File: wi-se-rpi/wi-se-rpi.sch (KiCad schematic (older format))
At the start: 43 parts, among them J1 RASPI, SW1 RESET, SW2 BOOT0, SW3 FLASH_EN_SW, U1 AMS1117-3.3, U2 ESP-WROOM-02, U3 MC74VHC1G, U4 NL27WZ00, U5 NL27WZ32

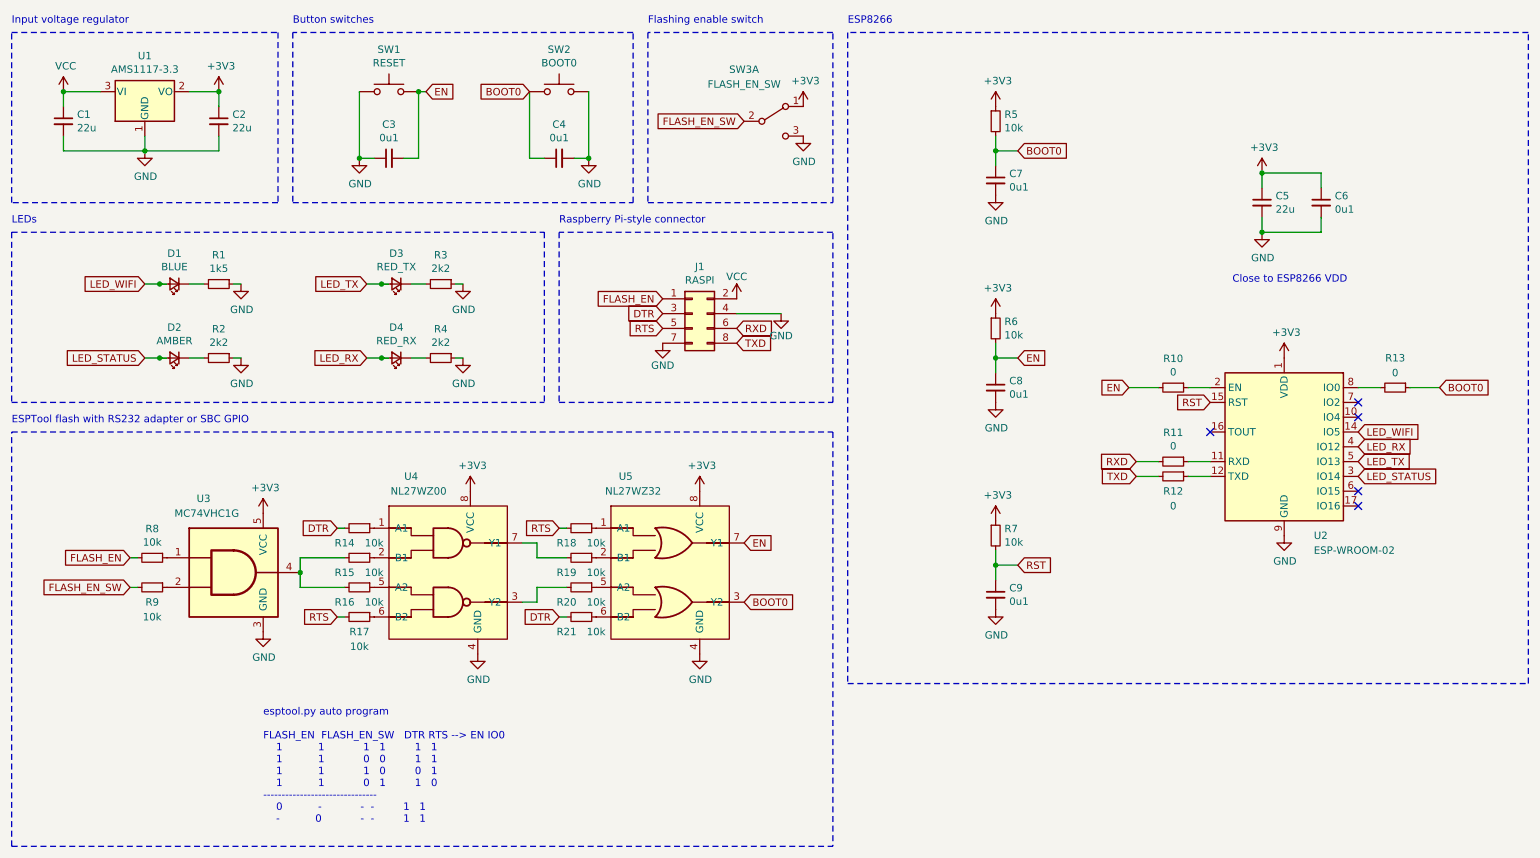
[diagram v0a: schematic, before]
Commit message: Make RPI version as small as it can be
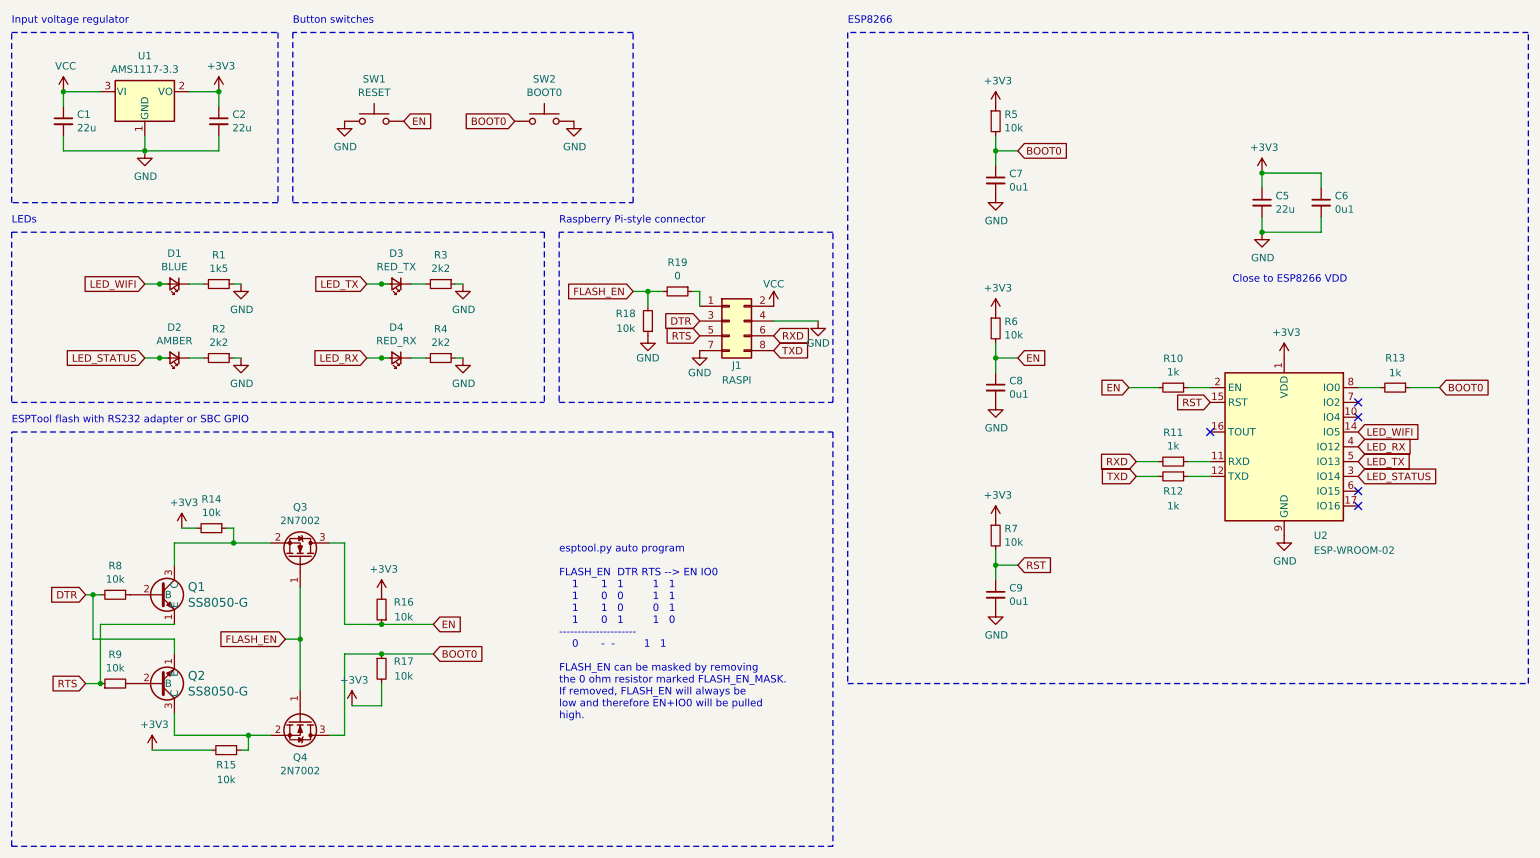
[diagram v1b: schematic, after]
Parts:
- removed C3, C4: 0u1, Capacitor_SMD:C_0603_1608Metric_Pad1.08x0.95mm_HandSolder, symbol Device:C_Small
- removed R20, R21: 10k, Resistor_SMD:R_0603_1608Metric_Pad0.98x0.95mm_HandSolder, symbol Device:R_Small
- removed SW3: FLASH_EN_SW, JS102011SCQN:CK-JS102011SCQN-0-0-0, symbol Switch:SW_DPDT_x2
- removed U3: MC74VHC1G, ON-gates:SOT95P280X145-5N, symbol Logic_Gates:MC74VHC1G
- removed U4: NL27WZ00, ON-gates:SOP50P310X90-8N, symbol Logic_Gates:NL27WZ00
- removed U5: NL27WZ32, ON-gates:SOP50P310X90-8N, symbol Logic_Gates:NL27WZ32
- added Q1, Q2: SS8050-G, SS8050-G:SS8050-G, symbol SS8050-G:SS8050-G
- added Q3, Q4: 2N7002, Package_TO_SOT_SMD:SOT-23, symbol Transistor_FET:2N7002
- C1, C2, C5: footprint Capacitor_SMD:C_1206_3216Metric_Pad1.33x1.80mm_HandSolder -> Capacitor_SMD:C_1206_3216Metric
- C6: footprint Capacitor_SMD:C_0603_1608Metric_Pad1.08x0.95mm_HandSolder -> Capacitor_SMD:C_0603_1608Metric
- C7, C8, C9: footprint Capacitor_SMD:C_0603_1608Metric_Pad1.08x0.95mm_HandSolder -> Capacitor_SMD:C_0402_1005Metric
- R1, R14, R15, R16, R17, R18, R2, R3, R4, R5, R6, R7, R8, R9: footprint Resistor_SMD:R_0603_1608Metric_Pad0.98x0.95mm_HandSolder -> Resistor_SMD:R_0402_1005Metric
- R10, R11, R12, R13: value 0 -> 1k; footprint Resistor_SMD:R_0603_1608Metric_Pad0.98x0.95mm_HandSolder -> Resistor_SMD:R_0402_1005Metric
- R19: value 10k -> 0
- SW1, SW2: footprint Button_Switch_SMD:SW_SPST_B3U-3100P -> wi-se:SW_SPST_B3U-3100P_silk_change
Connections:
- net labels removed: FLASH_EN_SW
- wire segments 74 -> 87
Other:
- note added: "esptool.py auto program\n\nFLASH_EN DTR RTS --> EN IO0\n 1 1 1 1 1\n 1 0 0 1 1\n 1 1 0 0 1\n 1 0 1 1 0\n---------------------\n 0 - - 1 1 \n\nFLASH_EN can be masked by removing\nthe 0 ohm resistor marked FLASH_EN_MASK.\nIf removed, FLASH_EN will always be\nlow and therefore EN+IO0 will be pulled\nhigh."
- note removed: "Flashing enable switch"
- note removed: "esptool.py auto program\n\nFLASH_EN FLASH_EN_SW DTR RTS --> EN IO0\n 1 1 1 1 1 1\n 1 1 0 0 1 1\n 1 1 1 0 0 1\n 1 1 0 1 1 0\n-------------------------------\n 0 - - - 1 1\n - 0 - - 1 1\n"
- moved on the sheet: J1, SW1, SW2

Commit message: Final version of rpi variant (last famous words)
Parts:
- C1, C2, C5: value 22u -> 10u; LCSC Part (none) -> C13585
- C6: LCSC Part (none) -> C14663
- C7, C8, C9: LCSC Part (none) -> C1546
- Q1, Q2: LCSC Part (none) -> C2150
- Q3, Q4: LCSC Part (none) -> C8545
- R1: LCSC Part (none) -> C25867
- R10, R11, R12, R13: LCSC Part (none) -> C11702
- R14, R15, R16, R17, R18, R5, R6, R7, R8, R9: LCSC Part (none) -> C25744
- R19: LCSC Part (none) -> C17168
- R2, R3, R4: LCSC Part (none) -> C25879
- U1: LCSC Part (none) -> C6186
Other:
- note added: "esptool.py auto program\n\nFLASH_EN DTR RTS --> EN IO0\n 1 1 1 1 1\n 1 0 0 1 1\n 1 1 0 0 1\n 1 0 1 1 0\n---------------------\n 0 - - 1 1 \n\nFLASH_EN can be masked by removing\nthe 0 ohm resistor marked "FLEN disable".\nIf removed, FLASH_EN will always be\nlow and therefore EN+IO0 will be pulled\nhigh."
- note removed: "esptool.py auto program\n\nFLASH_EN DTR RTS --> EN IO0\n 1 1 1 1 1\n 1 0 0 1 1\n 1 1 0 0 1\n 1 0 1 1 0\n---------------------\n 0 - - 1 1 \n\nFLASH_EN can be masked by removing\nthe 0 ohm resistor marked FLASH_EN_MASK.\nIf removed, FLASH_EN will always be\nlow and therefore EN+IO0 will be pulled\nhigh."
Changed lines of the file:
@@
 Sheet 1 1
 Title "Wi-Se ESP8266 - Raspberry Pi-style header version"
-Date "2021-01-14"
+Date "2021-01-18"
 Rev "v0.1"
 Comp "Davide Depau"
@@
 F 2 "Package_TO_SOT_SMD:SOT-223-3_TabPin2" H 1550 1350 50  0001 C CNN
 F 3 "http://www.advanced-monolithic.com/pdf/ds1117.pdf" H 1650 900 50  0001 C CNN
+F 4 "C6186" H 1550 1150 50  0001 C CNN "LCSC Part"
 	1    1550 1150
 	1    0    0    -1
@@
 P 1000 1350
 F 0 "C1" H 1092 1396 50  0000 L CNN
-F 1 "22u" H 1092 1305 50  0000 L CNN
+F 1 "10u" H 1092 1305 50  0000 L CNN
 F 2 "Capacitor_SMD:C_1206_3216Metric" H 1000 1350 50  0001 C CNN
 F 3 "~" H 1000 1350 50  0001 C CNN
+F 4 "C13585" H 1000 1350 50  0001 C CNN "LCSC Part"
 	1    1000 1350
 	1    0    0    -1
@@
 P 2050 1350
 F 0 "C2" H 2142 1396 50  0000 L CNN
-F 1 "22u" H 2142 1305 50  0000 L CNN
+F 1 "10u" H 2142 1305 50  0000 L CNN
 F 2 "Capacitor_SMD:C_1206_3216Metric" H 2050 1350 50  0001 C CNN
 F 3 "~" H 2050 1350 50  0001 C CNN
+F 4 "C13585" H 2050 1350 50  0001 C CNN "LCSC Part"
 	1    2050 1350
 	1    0    0    -1
@@
 F 2 "Resistor_SMD:R_0402_1005Metric" H 2050 2450 50  0001 C CNN
 F 3 "~" H 2050 2450 50  0001 C CNN
+F 4 "C25867" H 2050 2450 50  0001 C CNN "LCSC Part"
 	1    2050 2450
 	0    1    1    0
@@
 F 2 "Resistor_SMD:R_0402_1005Metric" H 2050 2950 50  0001 C CNN
 F 3 "~" H 2050 2950 50  0001 C CNN
+F 4 "C25879" H 2050 2950 50  0001 C CNN "LCSC Part"
 	1    2050 2950
 	0    1    1    0
@@
 F 2 "Resistor_SMD:R_0402_1005Metric" H 3550 2450 50  0001 C CNN
 F 3 "~" H 3550 2450 50  0001 C CNN
+F 4 "C25879" H 3550 2450 50  0001 C CNN "LCSC Part"
 	1    3550 2450
 	0    1    1    0
@@
 F 2 "Resistor_SMD:R_0402_1005Metric" H 3550 2950 50  0001 C CNN
 F 3 "~" H 3550 2950 50  0001 C CNN
+F 4 "C25879" H 3550 2950 50  0001 C CNN "LCSC Part"
 	1    3550 2950
 	0    1    1    0
@@
 P 9100 1900
 F 0 "C5" H 9192 1946 50  0000 L CNN
-F 1 "22u" H 9192 1855 50  0000 L CNN
+F 1 "10u" H 9192 1855 50  0000 L CNN
 F 2 "Capacitor_SMD:C_1206_3216Metric" H 9100 1900 50  0001 C CNN
 F 3 "~" H 9100 1900 50  0001 C CNN
+F 4 "C13585" H 9100 1900 50  0001 C CNN "LCSC Part"
 	1    9100 1900
 	1    0    0    -1
@@
 F 2 "Capacitor_SMD:C_0603_1608Metric" H 9500 1900 50  0001 C CNN
 F 3 "~" H 9500 1900 50  0001 C CNN
+F 4 "C14663" H 9500 1900 50  0001 C CNN "LCSC Part"
 	1    9500 1900
 	1    0    0    -1
@@
 F 2 "Resistor_SMD:R_0402_1005Metric" H 7300 1350 50  0001 C CNN
 F 3 "~" H 7300 1350 50  0001 C CNN
+F 4 "C25744" H 7300 1350 50  0001 C CNN "LCSC Part"
 	1    7300 1350
 	1    0    0    -1
@@
 F 2 "Resistor_SMD:R_0402_1005Metric" H 7300 2750 50  0001 C CNN
 F 3 "~" H 7300 2750 50  0001 C CNN
+F 4 "C25744" H 7300 2750 50  0001 C CNN "LCSC Part"
 	1    7300 2750
 	1    0    0    -1
@@
 F 2 "Resistor_SMD:R_0402_1005Metric" H 7300 4150 50  0001 C CNN
 F 3 "~" H 7300 4150 50  0001 C CNN
+F 4 "C25744" H 7300 4150 50  0001 C CNN "LCSC Part"
 	1    7300 4150
 	1    0    0    -1
@@
 F 2 "Capacitor_SMD:C_0402_1005Metric" H 7300 1750 50  0001 C CNN
 F 3 "~" H 7300 1750 50  0001 C CNN
+F 4 "C1546" H 7300 1750 50  0001 C CNN "LCSC Part"
 	1    7300 1750
 	1    0    0    -1
@@
 F 2 "Capacitor_SMD:C_0402_1005Metric" H 7300 3150 50  0001 C CNN
 F 3 "~" H 7300 3150 50  0001 C CNN
+F 4 "C1546" H 7300 3150 50  0001 C CNN "LCSC Part"
 	1    7300 3150
 	1    0    0    -1
@@
 F 2 "Capacitor_SMD:C_0402_1005Metric" H 7300 4550 50  0001 C CNN
 F 3 "~" H 7300 4550 50  0001 C CNN
+F 4 "C1546" H 7300 4550 50  0001 C CNN "LCSC Part"
 	1    7300 4550
 	1    0    0    -1
@@
 F 2 "Resistor_SMD:R_0402_1005Metric" H 8500 3650 50  0001 C CNN
 F 3 "~" H 8500 3650 50  0001 C CNN
+F 4 "C11702" H 8500 3650 50  0001 C CNN "LCSC Part"
 	1    8500 3650
 	0    1    1    0
@@
 F 2 "Resistor_SMD:R_0402_1005Metric" H 8500 3750 50  0001 C CNN
 F 3 "~" H 8500 3750 50  0001 C CNN
+F 4 "C11702" H 8500 3750 50  0001 C CNN "LCSC Part"
 	1    8500 3750
 	0    1    1    0
@@
 F 2 "Resistor_SMD:R_0402_1005Metric" H 8500 3150 50  0001 C CNN
 F 3 "~" H 8500 3150 50  0001 C CNN
+F 4 "C11702" H 8500 3150 50  0001 C CNN "LCSC Part"
 	1    8500 3150
 	0    1    1    0
@@
 F 2 "Resistor_SMD:R_0402_1005Metric" H 10000 3150 50  0001 C CNN
 F 3 "~" H 10000 3150 50  0001 C CNN
+F 4 "C11702" H 10000 3150 50  0001 C CNN "LCSC Part"
 	1    10000 3150
 	0    1    1    0
@@
 ESPTool flash with RS232 adapter or SBC GPIO
 Text Notes 4350 5400 0    50   ~ 0
-    esptool.py auto program\n\nFLASH_EN  DTR RTS --> EN IO0\n    1       1   1         1   1\n    1       0   0         1   1\n    1       1   0         0   1\n    1       0   1         1   0\n---------------------\n    0       -  -         1   1 \n\nFLASH_EN can be masked by removing\nthe 0 ohm resistor marked FLASH_EN_MASK.\nIf removed, FLASH_EN will always be\nlow and therefore EN+IO0 will be pulled\nhigh.
+    esptool.py auto program\n\nFLASH_EN  DTR RTS --> EN IO0\n    1       1   1         1   1\n    1       0   0         1   1\n    1       1   0         0   1\n    1       0   1         1   0\n---------------------\n    0       -  -         1   1 \n\nFLASH_EN can be masked by removing\nthe 0 ohm resistor marked "FLEN disable".\nIf removed, FLASH_EN will always be\nlow and therefore EN+IO0 will be pulled\nhigh.
 Wire Notes Line
 	4250 2100 4250 3250
@@
 F 2 "Package_TO_SOT_SMD:SOT-23" H 2800 5325 50  0001 L CIN
 F 3 "https://www.onsemi.com/pub/Collateral/NDS7002A-D.PDF" H 2600 5400 50  0001 L CNN
+F 4 "C8545" H 2600 5400 50  0001 C CNN "LCSC Part"
 	1    2600 5400
 	0    1    1    0
@@
 F 2 "SS8050-G:SS8050-G" H 1900 4450 60  0001 L CNN
 F 3 "" H 1550 4550 60  0000 C CNN
+F 4 "C2150" H 1650 4550 50  0001 C CNN "LCSC Part"
 	1    1650 4550
 	1    0    0    -1
@@
 F 2 "SS8050-G:SS8050-G" H 1900 5050 60  0001 L CNN
 F 3 "" H 1550 5150 60  0000 C CNN
+F 4 "C2150" H 1650 5150 50  0001 C CNN "LCSC Part"
 	1    1650 5150
 	1    0    0    1
@@
 F 2 "Resistor_SMD:R_0402_1005Metric" H 1350 4550 50  0001 C CNN
 F 3 "~" H 1350 4550 50  0001 C CNN
+F 4 "C25744" H 1350 4550 50  0001 C CNN "LCSC Part"
 	1    1350 4550
 	0    1    1    0
@@
 F 2 "Resistor_SMD:R_0402_1005Metric" H 1350 5150 50  0001 C CNN
 F 3 "~" H 1350 5150 50  0001 C CNN
+F 4 "C25744" H 1350 5150 50  0001 C CNN "LCSC Part"
 	1    1350 5150
 	0    -1   -1   0
@@
 F 2 "Resistor_SMD:R_0402_1005Metric" H 2000 4100 50  0001 C CNN
 F 3 "~" H 2000 4100 50  0001 C CNN
+F 4 "C25744" H 2000 4100 50  0001 C CNN "LCSC Part"
 	1    2000 4100
 	0    1    1    0
@@
 F 2 "Resistor_SMD:R_0402_1005Metric" H 2100 5600 50  0001 C CNN
 F 3 "~" H 2100 5600 50  0001 C CNN
+F 4 "C25744" H 2100 5600 50  0001 C CNN "LCSC Part"
 	1    2100 5600
 	0    1    1    0
@@
 F 2 "Package_TO_SOT_SMD:SOT-23" H 2800 4225 50  0001 L CIN
 F 3 "https://www.onsemi.com/pub/Collateral/NDS7002A-D.PDF" H 2600 4300 50  0001 L CNN
+F 4 "C8545" H 2600 4300 50  0001 C CNN "LCSC Part"
 	1    2600 4300
 	0    1    -1   0
@@
 F 2 "Resistor_SMD:R_0402_1005Metric" H 3150 4650 50  0001 C CNN
 F 3 "~" H 3150 4650 50  0001 C CNN
+F 4 "C25744" H 3150 4650 50  0001 C CNN "LCSC Part"
 	1    3150 4650
 	-1   0    0    1
@@
 F 2 "Resistor_SMD:R_0402_1005Metric" H 3150 5050 50  0001 C CNN
 F 3 "~" H 3150 5050 50  0001 C CNN
+F 4 "C25744" H 3150 5050 50  0001 C CNN "LCSC Part"
 	1    3150 5050
 	1    0    0    -1
@@
 F 2 "Resistor_SMD:R_0402_1005Metric" H 4950 2700 50  0001 C CNN
 F 3 "~" H 4950 2700 50  0001 C CNN
+F 4 "C25744" H 4950 2700 50  0001 C CNN "LCSC Part"
 	1    4950 2700
 	-1   0    0    1
@@
 F 2 "Resistor_SMD:R_0603_1608Metric_Pad0.98x0.95mm_HandSolder" H 5150 2500 50  0001 C CNN
 F 3 "~" H 5150 2500 50  0001 C CNN
+F 4 "C17168" H 5150 2500 50  0001 C CNN "LCSC Part"
 	1    5150 2500
 	0    1    1    0

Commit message: Replace buttons with cheap aliexpress ones
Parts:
- SW1, SW2: footprint wi-se:SW_SPST_B3U-3100P_silk_change -> aliexpress-switch:Tactile_Push_Button_SMD_3x3x1.5mm.kicad_mod
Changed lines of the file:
@@
 F 0 "SW1" H 3100 1635 50  0000 C CNN
 F 1 "RESET" H 3100 1544 50  0000 C CNN
-F 2 "wi-se:SW_SPST_B3U-3100P_silk_change" H 3100 1550 50  0001 C CNN
+F 2 "aliexpress-switch:Tactile_Push_Button_SMD_3x3x1.5mm.kicad_mod" H 3100 1550 50  0001 C CNN
 F 3 "~" H 3100 1550 50  0001 C CNN
 	1    3100 1350
@@
 F 0 "SW2" H 4250 1635 50  0000 C CNN
 F 1 "BOOT0" H 4250 1544 50  0000 C CNN
-F 2 "wi-se:SW_SPST_B3U-3100P_silk_change" H 4250 1550 50  0001 C CNN
+F 2 "aliexpress-switch:Tactile_Push_Button_SMD_3x3x1.5mm.kicad_mod" H 4250 1550 50  0001 C CNN
 F 3 "~" H 4250 1550 50  0001 C CNN
 	1    4250 1350

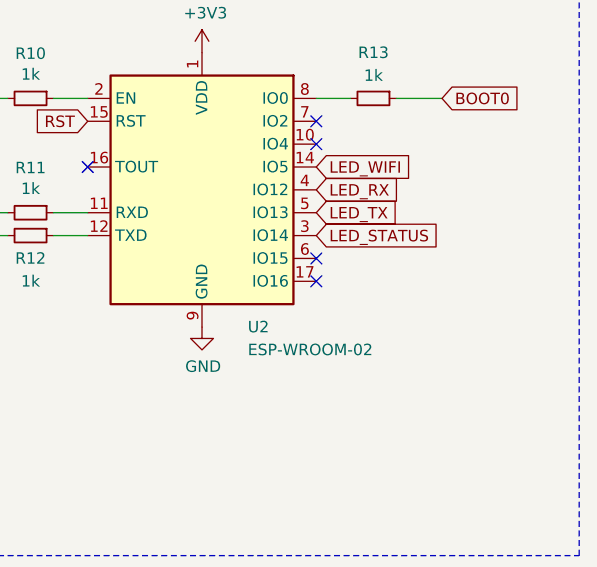
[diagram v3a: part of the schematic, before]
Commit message: rpi: Add missing GPIO15 pull-down
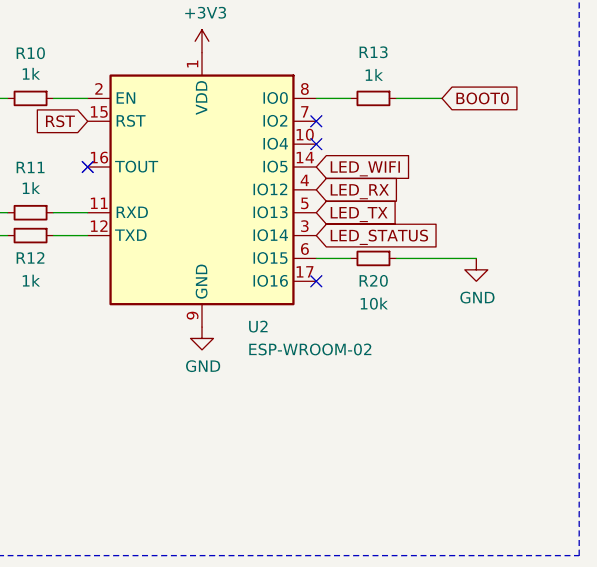
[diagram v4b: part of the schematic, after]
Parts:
- added R20: 10k, Resistor_SMD:R_0402_1005Metric, symbol Device:R_Small
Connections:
- wire segments 87 -> 89
- no-connect marks 5 -> 4
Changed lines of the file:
@@
 Sheet 1 1
 Title "Wi-Se ESP8266 - Raspberry Pi-style header version"
-Date "2021-01-18"
-Rev "v0.1"
+Date "2021-03-19"
+Rev "v0.2"
 Comp "Davide Depau"
 Comment1 "Raspberry Pi-compatible header pinout"
@@
 Comment4 ""
 $EndDescr
-$Comp
-L RF_Module:ESP-WROOM-02 U2
-U 1 1 5FFE38E5
-P 9250 3550
-F 0 "U2" H 9450 2950 50  0000 L CNN
-F 1 "ESP-WROOM-02" H 9450 2850 50  0000 L CNN
-F 2 "RF_Module:ESP-WROOM-02" H 9850 3000 50  0001 C CNN
-F 3 "https://www.espressif.com/sites/default/files/documentation/0c-esp-wroom-02_datasheet_en.pdf" H 9300 5050 50  0001 C CNN
-	1    9250 3550
-	1    0    0    -1
-$EndComp
 $Comp
 L Regulator_Linear:AMS1117-3.3 U1
@@
 Text GLabel 9750 3750 2    50   Input ~ 0
 LED_STATUS
-NoConn ~ 9750 3850
 NoConn ~ 9750 3350
 NoConn ~ 8750 3450
@@
 Wire Wire Line
 	5300 2500 5300 2600
+$Comp
+L RF_Module:ESP-WROOM-02 U2
+U 1 1 5FFE38E5
+P 9250 3550
+F 0 "U2" H 9450 2950 50  0000 L CNN
+F 1 "ESP-WROOM-02" H 9450 2850 50  0000 L CNN
+F 2 "RF_Module:ESP-WROOM-02" H 9850 3000 50  0001 C CNN
+F 3 "https://www.espressif.com/sites/default/files/documentation/0c-esp-wroom-02_datasheet_en.pdf" H 9300 5050 50  0001 C CNN
+	1    9250 3550
+	1    0    0    -1
+$EndComp
+$Comp
+L Device:R_Small R20
+U 1 1 60554303
+P 10000 3850
+F 0 "R20" V 10100 3850 50  0000 C CNN
+F 1 "10k" V 10200 3850 50  0000 C CNN
+F 2 "Resistor_SMD:R_0402_1005Metric" H 10000 3850 50  0001 C CNN
+F 3 "~" H 10000 3850 50  0001 C CNN
+F 4 "C25744" H 10000 3850 50  0001 C CNN "LCSC Part"
+	1    10000 3850
+	0    1    1    0
+$EndComp
+Wire Wire Line
+	9750 3850 9900 3850
+$Comp
+L power:GND #PWR06
+U 1 1 6055A1F4
+P 10450 3850
+F 0 "#PWR06" H 10450 3600 50  0001 C CNN
+F 1 "GND" H 10455 3677 50  0000 C CNN
+F 2 "" H 10450 3850 50  0001 C CNN
+F 3 "" H 10450 3850 50  0001 C CNN
+	1    10450 3850
+	1    0    0    -1
+$EndComp
+Wire Wire Line
+	10100 3850 10450 3850
 $EndSCHEMATC
